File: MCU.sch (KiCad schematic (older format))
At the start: 50 parts, among them CON1 BARREL_JACK, P1 CONN_01X14, P2 CONN_01X14, P3 CONN_01X09, P4 USB_OTG, P5 CONN_02X05, P6 CONN_01X09, P7 CONN_02X04, P8 USB_OTG, SW1 Reset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

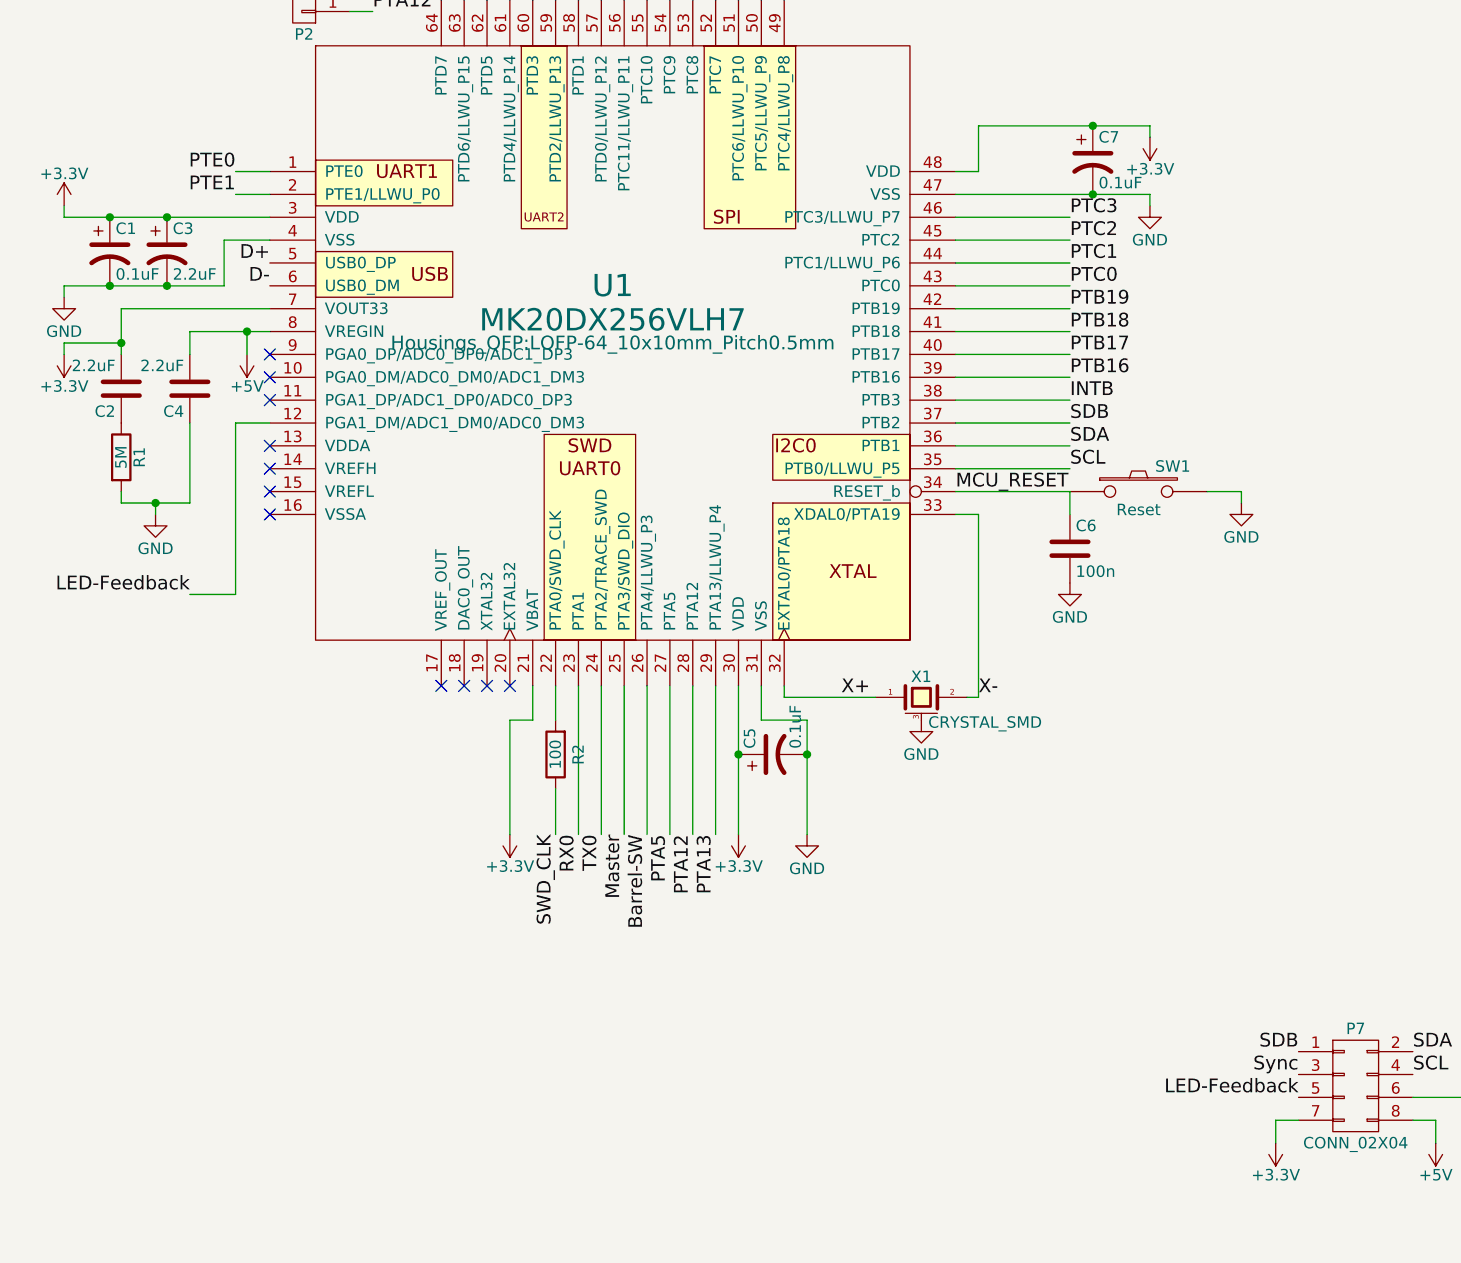
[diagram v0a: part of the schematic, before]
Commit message: Added Analog-Digital Conversion Capability
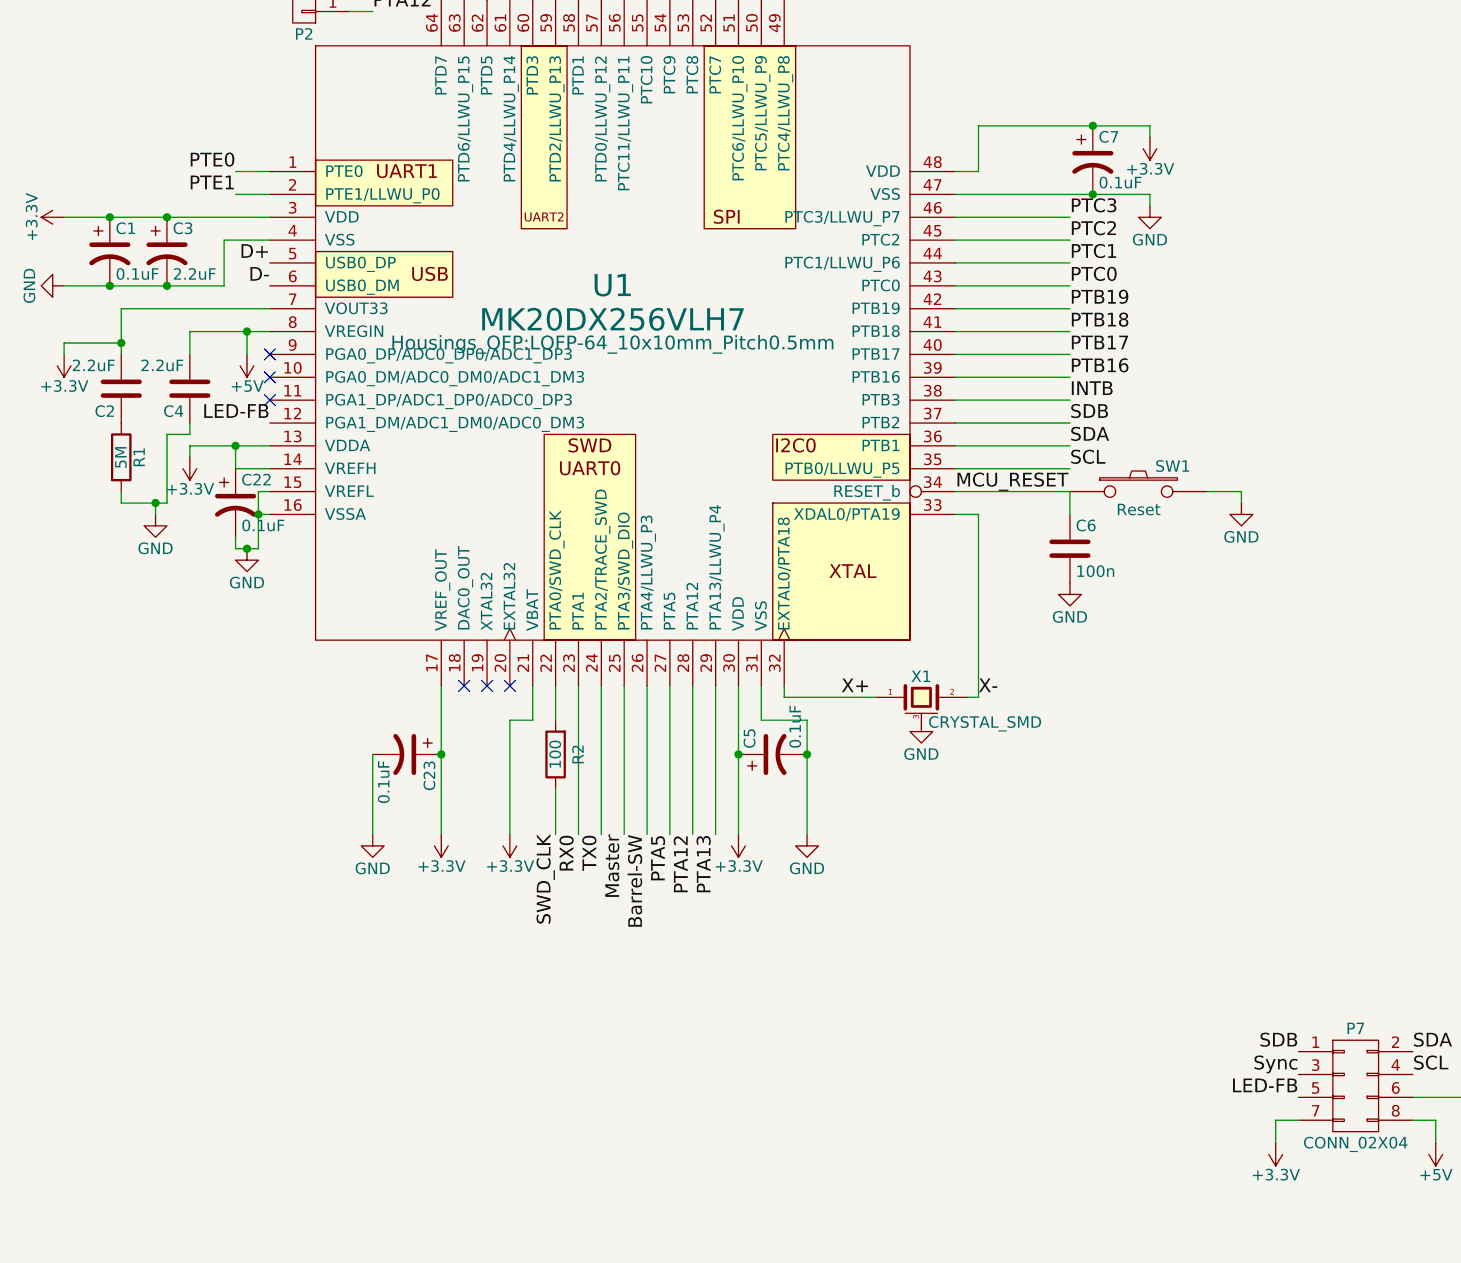
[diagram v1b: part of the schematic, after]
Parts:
- added C22, C23: 0.1uF, Capacitors_SMD:C_0603, symbol CP1
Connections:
- net +3V3: now also U1.13 (VDDA), U1.14 (VREFH), U1.17 (VREF_OUT), C22.1, C23.1
- net GND: now also U1.15 (VREFL), U1.16 (VSSA), C22.2, C23.2
- net LED-Feedback renamed LED-FB
- no-connect marks 23 -> 18
